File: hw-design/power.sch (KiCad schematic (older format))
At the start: 9 parts, among them P10 CONN_01X02, P3 CONN_01X03, U3 MCP73833, U4 AP111733

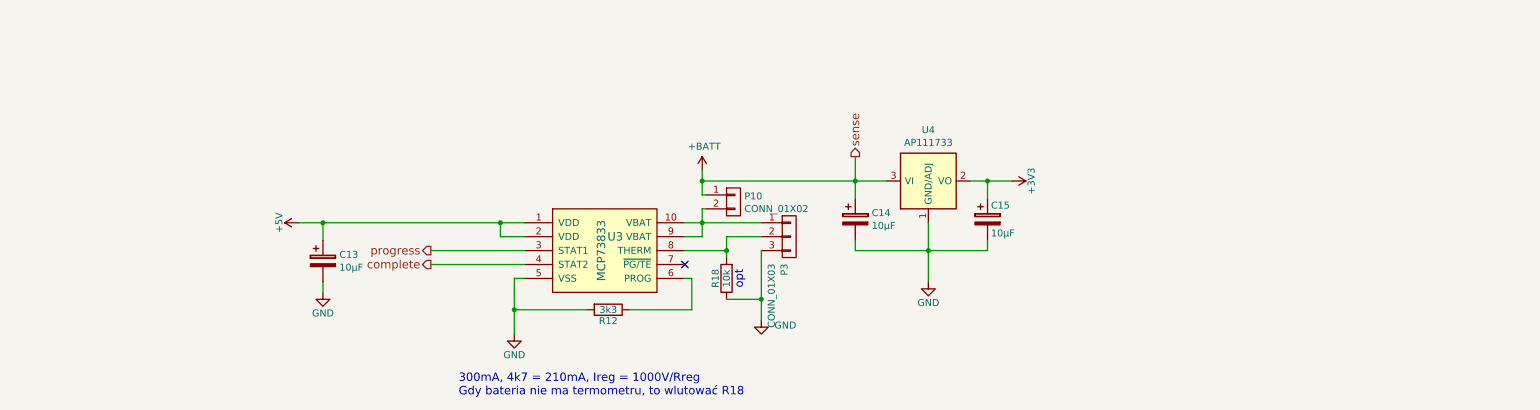
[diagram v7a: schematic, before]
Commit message: 3 boards split
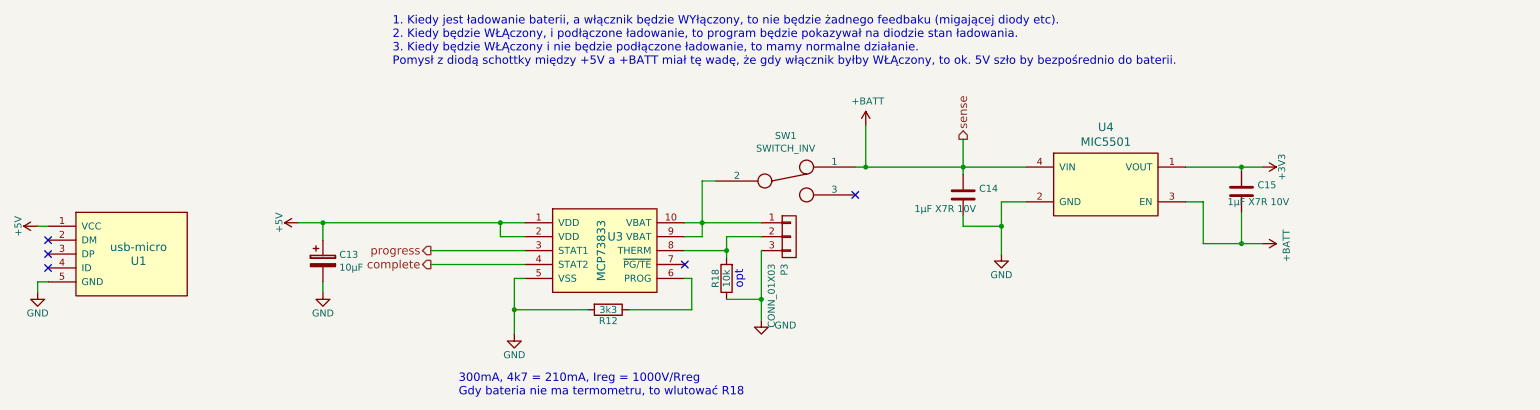
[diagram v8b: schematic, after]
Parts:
- removed C14, C15: 10µF, w_smd_cap:c_tant_B, symbol CP
- removed P10: CONN_01X02, w_pin_strip:pin_strip_2, symbol CONN_01X02
- removed U4: AP111733, linear:SOT223, symbol AP111733
- added C14, C15: 1µF X7R 10V, w_smd_cap:c_0603, symbol C
- added SW1: SWITCH_INV, iwasz:1437575-1, symbol SWITCH_INV
- added U1: usb-micro, w_conn_pc:conn_usb_B_micro_smd-2, symbol usb-micro
- added U4: MIC5501, w_smd_trans:sot23-5, symbol MIC5501
- R12, R18: footprint w_smd_resistors:r_0603 -> w_smd_resistors:r_0402
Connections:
- net +3V3: now also C15.1, U4.1 (VOUT)
- net +5V: now also U1.1 (VCC)
- net +BATT: now also C14.1, C15.2, SW1.1, U4.3 (EN), U4.4 (VIN)
- net GND: now also C14.2, U1.5 (GND), U4.2 (GND)
- net at P3.1 (P1), U3.10 (VBAT), U3.9 (VBAT): now also SW1.2
- no-connect marks 1 -> 5
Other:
- note added: "1. Kiedy jest ładowanie baterii, a włącznik będzie WYłączony, to nie będzie żadnego feedbaku (migającej diody etc). \n2. Kiedy będzie WŁĄczony, i podłączone ładowanie, to program będzie pokazywał na diodzie stan ładowania.\n3. Kiedy będzie WŁĄczony i nie będzie podłączone ładowanie, to mamy normalne działanie.\nPomysł z diodą schottky między +5V a +BATT miał tę wadę, że gdy włącznik byłby WŁĄczon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"
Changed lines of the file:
@@
 $Descr A4 11693 8268
 encoding utf-8
-Sheet 3 5
+Sheet 2 6
 Title ""
 Date ""
@@
 $EndDescr
 $Comp
-L CP C15
-U 1 1 5723EAD0
-P 8175 3300
-F 0 "C15" H 8200 3400 50  0000 L CNN
-F 1 "10µF" H 8200 3200 50  0000 L CNN
-F 2 "w_smd_cap:c_tant_B" H 8213 3150 30  0001 C CNN
-F 3 "" H 8175 3300 60  0000 C CNN
-	1    8175 3300
-	1    0    0    -1
-$EndComp
-Wire Wire Line
-	8050 3025 8350 3025
-Wire Wire Line
-	8175 3025 8175 3150
-$Comp
 L MCP73833 U3
 U 1 1 5723EAD1
@@
 	1    0    0    -1
 $EndComp
-$Comp
-L CP C14
-U 1 1 5723EAD2
-P 7225 3300
-F 0 "C14" H 7343 3346 50  0000 L CNN
-F 1 "10µF" H 7343 3254 50  0000 L CNN
-F 2 "w_smd_cap:c_tant_B" H 7263 3150 30  0001 C CNN
-F 3 "" H 7225 3300 60  0000 C CNN
-	1    7225 3300
-	1    0    0    -1
-$EndComp
 Wire Wire Line
 	3225 3325 4850 3325
@@
 	3400 3325 3400 3450
 $Comp
-L +5V #PWR22
+L +5V #PWR8
 U 1 1 5723EAD4
 P 3225 3325
-F 0 "#PWR22" H 3225 3175 50  0001 C CNN
+F 0 "#PWR8" H 3225 3175 50  0001 C CNN
 F 1 "+5V" H 3225 3465 50  0000 C CNN
 F 2 "" H 3225 3325 60  0000 C CNN
@@
 Connection ~ 3400 3325
 $Comp
-L GND #PWR23
+L GND #PWR9
 U 1 1 5723EAD5
 P 3400 3825
-F 0 "#PWR23" H 3400 3575 50  0001 C CNN
+F 0 "#PWR9" H 3400 3575 50  0001 C CNN
 F 1 "GND" H 3400 3675 50  0000 C CNN
 F 2 "" H 3400 3825 60  0000 C CNN
@@
 	4175 3625 4850 3625
 $Comp
-L GND #PWR24
+L GND #PWR10
 U 1 1 5723EAD6
 P 4775 4125
-F 0 "#PWR24" H 4775 3875 50  0001 C CNN
+F 0 "#PWR10" H 4775 3875 50  0001 C CNN
 F 1 "GND" H 4775 3975 50  0000 C CNN
 F 2 "" H 4775 4125 60  0000 C CNN
@@
 	4775 3725 4775 4125
 $Comp
-L GND #PWR27
+L GND #PWR13
 U 1 1 5723EAD7
-P 7750 3750
-F 0 "#PWR27" H 7750 3500 50  0001 C CNN
-F 1 "GND" H 7750 3600 50  0000 C CNN
-F 2 "" H 7750 3750 60  0000 C CNN
-F 3 "" H 7750 3750 60  0000 C CNN
-	1    7750 3750
-	1    0    0    -1
-$EndComp
-Wire Wire Line
-	7225 3450 7225 3525
-Wire Wire Line
-	7225 3525 8175 3525
-Wire Wire Line
-	8175 3525 8175 3450
-Wire Wire Line
-	7750 3325 7750 3750
-Connection ~ 7750 3525
-$Comp
-L +3V3 #PWR28
+P 8275 3550
+F 0 "#PWR13" H 8275 3300 50  0001 C CNN
+F 1 "GND" H 8275 3400 50  0000 C CNN
+F 2 "" H 8275 3550 60  0000 C CNN
+F 3 "" H 8275 3550 60  0000 C CNN
+	1    8275 3550
+	1    0    0    -1
+$EndComp
+$Comp
+L +3V3 #PWR14
 U 1 1 5723EAD8
-P 8350 3025
-F 0 "#PWR28" H 8350 2875 50  0001 C CNN
-F 1 "+3V3" H 8350 3165 50  0000 C CNN
-F 2 "" H 8350 3025 60  0000 C CNN
-F 3 "" H 8350 3025 60  0000 C CNN
-	1    8350 3025
+P 10150 2925
+F 0 "#PWR14" H 10150 2775 50  0001 C CNN
+F 1 "+3V3" H 10150 3065 50  0000 C CNN
+F 2 "" H 10150 2925 60  0000 C CNN
+F 3 "" H 10150 2925 60  0000 C CNN
+	1    10150 2925
 	0    1    1    0
 $EndComp
-Connection ~ 8175 3025
 $Comp
 L R R12
@@
 F 0 "R12" V 5530 3950 50  0000 C CNN
 F 1 "3k3" V 5450 3950 50  0000 C CNN
-F 2 "w_smd_resistors:r_0603" V 5380 3950 30  0001 C CNN
+F 2 "w_smd_resistors:r_0402" V 5380 3950 30  0001 C CNN
 F 3 "" H 5450 3950 30  0000 C CNN
 	1    5450 3950
@@
 Connection ~ 6125 3325
 $Comp
-L GND #PWR26
+L GND #PWR11
 U 1 1 5723EADB
 P 6550 4025
-F 0 "#PWR26" H 6550 3775 50  0001 C CNN
+F 0 "#PWR11" H 6550 3775 50  0001 C CNN
 F 1 "GND" H 6644 3988 50  0000 L CNN
 F 2 "" H 6550 4025 60  0000 C CNN
@@
 Wire Wire Line
 	6300 3525 6000 3525
-Connection ~ 7225 3025
-Wire Wire Line
-	6125 2950 6125 3125
-Wire Wire Line
-	6125 3225 6125 3425
+Wire Wire Line
+	7300 2625 7300 2925
+Wire Wire Line
+	6125 3025 6125 3425
 Wire Wire Line
 	6300 3425 6300 3575
 Wire Wire Line
 	6550 3525 6550 4025
-$Comp
-L AP111733 U4
-U 1 1 57241BB2
-P 7750 3025
-F 0 "U4" H 7750 3392 50  0000 C CNN
-F 1 "AP111733" H 7750 3301 50  0000 C CNN
-F 2 "linear:SOT223" H 7750 2675 50  0001 C CNN
-F 3 "" H 7850 2775 50  0000 C CNN
-	1    7750 3025
-	1    0    0    -1
-$EndComp
 NoConn ~ 6000 3625
 Wire Wire Line
 	6300 3425 6550 3425
-Connection ~ 6125 3025
+Connection ~ 7300 2925
 Text HLabel 4175 3525 0    60   Output ~ 0
 progress
 Text HLabel 4175 3625 0    60   Output ~ 0
 complete
-Text HLabel 7225 2850 1    60   Output ~ 0
+Text HLabel 8000 2725 1    60   Output ~ 0
 sense
 $Comp
-L +BATT #PWR25
+L +BATT #PWR12
 U 1 1 572542F4
-P 6125 2950
-F 0 "#PWR25" H 6125 2800 50  0001 C CNN
-F 1 "+BATT" H 6140 3123 50  0000 C CNN
-F 2 "" H 6125 2950 50  0000 C CNN
-F 3 "" H 6125 2950 50  0000 C CNN
-	1    6125 2950
-	1    0    0    -1
-$EndComp
-$Comp
-L CONN_01X02 P10
-U 1 1 577EA8A3
-P 6350 3175
-F 0 "P10" H 6428 3216 50  0000 L CNN
-F 1 "CONN_01X02" H 6428 3125 50  0000 L CNN
-F 2 "w_pin_strip:pin_strip_2" V 6178 3037 50  0001 R CNN
-F 3 "" H 6350 3175 50  0000 C CNN
-	1    6350 3175
+P 7300 2625
+F 0 "#PWR12" H 7300 2475 50  0001 C CNN
+F 1 "+BATT" H 7315 2798 50  0000 C CNN
+F 2 "" H 7300 2625 50  0000 C CNN
+F 3 "" H 7300 2625 50  0000 C CNN
+	1    7300 2625
 	1    0    0    -1
 $EndComp
@@
 	6000 3325 6550 3325
 Wire Wire Line
-	6125 3125 6150 3125
-Wire Wire Line
-	6125 3225 6150 3225
+	6125 3025 6225 3025
 $Comp
 L R R18
@@
 F 0 "R18" V 6380 3725 50  0000 C CNN
 F 1 "10k" V 6300 3725 50  0000 C CNN
-F 2 "w_smd_resistors:r_0603" V 6230 3725 30  0001 C CNN
+F 2 "w_smd_resistors:r_0402" V 6230 3725 30  0001 C CNN
 F 3 "" H 6300 3725 30  0000 C CNN
 	1    6300 3725
@@
 opt
 Wire Wire Line
-	6125 3025 7450 3025
-Wire Wire Line
-	7225 2850 7225 3150
-Wire Wire Line
 	4675 3425 4675 3325
+$Comp
+L usb-micro U1
+U 1 1 57D9F1F1
+P 2025 3500
+F 0 "U1" H 2075 3400 60  0000 C CNN
+F 1 "usb-micro" H 2075 3500 60  0000 C CNN
+F 2 "w_conn_pc:conn_usb_B_micro_smd-2" H 2075 3500 60  0001 C CNN
+F 3 "" H 2075 3500 60  0000 C CNN
+	1    2025 3500
+	1    0    0    -1
+$EndComp
+$Comp
+L GND #PWR7
+U 1 1 57D9F1F8
+P 1350 3825
+F 0 "#PWR7" H 1350 3575 50  0001 C CNN
+F 1 "GND" H 1350 3675 50  0000 C CNN
+F 2 "" H 1350 3825 60  0000 C CNN
+F 3 "" H 1350 3825 60  0000 C CNN
+	1    1350 3825
+	1    0    0    -1
+$EndComp
+Wire Wire Line
+	1425 3750 1350 3750
+Wire Wire Line
+	1350 3750 1350 3825
+NoConn ~ 1425 3650
+$Comp
+L +5V #PWR6
+U 1 1 57D9F201
+P 1350 3350
+F 0 "#PWR6" H 1350 3200 50  0001 C CNN
+F 1 "+5V" H 1350 3490 50  0000 C CNN
+F 2 "" H 1350 3350 60  0000 C CNN
+F 3 "" H 1350 3350 60  0000 C CNN
+	1    1350 3350
+	0    -1   -1   0
+$EndComp
+NoConn ~ 1425 3550
+NoConn ~ 1425 3450
+Wire Wire Line
+	1350 3350 1425 3350
+$Comp
+L SWITCH_INV SW1
+U 1 1 58099999
+P 6725 3025
+F 0 "SW1" H 6725 3350 50  0000 C CNN
+F 1 "SWITCH_INV" H 6725 3259 50  0000 C CNN
+F 2 "iwasz:1437575-1" H 6725 3025 50  0001 C CNN
+F 3 "http://pl.farnell.com/te-connectivity-alcoswitch/1437575-1/slide-switch-spdt-0-3a-4v-smd/dp/2468745" H 6725 3025 50  0001 C CNN
+F 4 "https://www.aliexpress.com/item/20pcs-MSK12C02-MINI-Miniature-SMD-Slide-Switch-1P2T-7Pin-For-DIY-Electronic-Accessories/32668282935.html?spm=2114.01010208.3.27.ooisEG&ws_ab_test=searchweb0_0,searchweb201602_4_10065_10068_10069_10084_10083_10017_10080_10082_10081_10060_10061_10062_10056_10055_10054_10059_10078_10079_10073_10070_421_420_10052_10053_10050_10051,searchweb201603_1&btsid=5d866a43-1c6b-482f-9d0d-8e6905bf5cb0" H 6725 3025 60  0001 C CNN "Datasheet2"
+F 5 "Włącznik zasilania" H 6725 3025 60  0001 C CNN "Opis"
+F 6 "http://www.farnell.com/cad/1839720.pdf?_ga=1.15575920.734114644.1428524414" H 6725 3025 60  0001 C CNN "DatasheetPDF"
+	1    6725 3025
+	1    0    0    -1
+$EndComp
+NoConn ~ 7225 3125
+Text Notes 3900 2200 0    60   ~ 0
+1. Kiedy jest ładowanie baterii, a włącznik będzie WYłączony, to nie będzie żadnego feedbaku (migającej diody etc). \n2. Kiedy będzie WŁĄczony, i podłączone ładowanie, to program będzie pokazywał na diodzie stan ładowania.\n3. Kiedy będzie WŁĄczony i nie będzie podłączone ładowanie, to mamy normalne działanie.\nPomysł z diodą schottky między +5V a +BATT miał tę wadę, że gdy włącznik byłby WŁĄczony, to ok. 5V szło by bezpośrednio do baterii.
+$Comp
+L MIC5501 U4
+U 1 1 580E915A
+P 9000 3075
+F 0 "U4" H 9025 3512 60  0000 C CNN
+F 1 "MIC5501" H 9025 3406 60  0000 C CNN
+F 2 "w_smd_trans:sot23-5" H 9000 3075 60  0001 C CNN
+F 3 "http://pl.farnell.com/microchip/mic5504-3-3ym5-tr/ldo-volt-reg-0-3a-3-3v-sot-23/dp/2510377" H 9000 3075 60  0001 C CNN
+	1    9000 3075
+	1    0    0    -1
+$EndComp
+Wire Wire Line
+	7225 2925 8450 2925
+Wire Wire Line
+	8450 3175 8275 3175
+Wire Wire Line
+	8275 3175 8275 3550
+Wire Wire Line
+	9600 2925 10150 2925
+Connection ~ 8000 2925
+$Comp
+L +BATT #PWR15
+U 1 1 580EB925
+P 10150 3475
+F 0 "#PWR15" H 10150 3325 50  0001 C CNN
+F 1 "+BATT" H 10165 3648 50  0000 C CNN
+F 2 "" H 10150 3475 50  0000 C CNN
+F 3 "" H 10150 3475 50  0000 C CNN
+	1    10150 3475
+	0    1    1    0
+$EndComp
+$Comp
+L C C14
+U 1 1 580EBC95
+P 8000 3125
+F 0 "C14" H 8115 3171 50  0000 L CNN
+F 1 "1µF X7R 10V" H 7650 3025 50  0000 L CNN
+F 2 "w_smd_cap:c_0603" H 8038 2975 50  0001 C CNN
+F 3 "" H 8000 3125 50  0000 C CNN
+	1    8000 3125
+	1    0    0    -1
+$EndComp
+Wire Wire Line
+	8000 2725 8000 2975
+Wire Wire Line
+	8000 3275 8000 3350
+Wire Wire Line
+	8000 3350 8275 3350
+Connection ~ 8275 3350
+$Comp
+L C C15
+U 1 1 580EC251
+P 10000 3100
+F 0 "C15" H 10115 3146 50  0000 L CNN
+F 1 "1µF X7R 10V" H 9900 3025 50  0000 L CNN
+F 2 "w_smd_cap:c_0603" H 10038 2950 50  0001 C CNN
+F 3 "" H 10000 3100 50  0000 C CNN
+	1    10000 3100
+	1    0    0    -1
+$EndComp
+Wire Wire Line
+	9600 3175 9725 3175
+Wire Wire Line
+	9725 3175 9725 3475
+Wire Wire Line
+	9725 3475 10150 3475
+Wire Wire Line
+	10000 3250 10000 3475
+Connection ~ 10000 3475
+Wire Wire Line
+	10000 2950 10000 2925
+Connection ~ 10000 2925
 $EndSCHEMATC
